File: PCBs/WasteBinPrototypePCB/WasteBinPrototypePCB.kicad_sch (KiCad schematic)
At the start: 31 parts, among them J1 Jack-DC 12V, J2 Conn_01x10_Male, J3 Conn_01x06_Male, J4 SM04B-SRSS-TB(LF)(SN), Q1 MMBT3904, Q2 IRL540NSTRLPBF, U1 PC817, U2 TLV1117-50, U3 ESP32-C3-DEVKITC-02, U4 A1301EUA-T

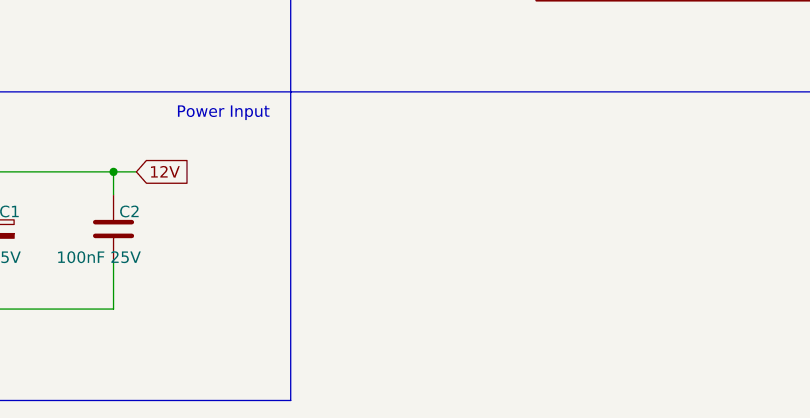
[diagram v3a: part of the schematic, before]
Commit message: created pcb board outline, layed out components and starting retouing wires.
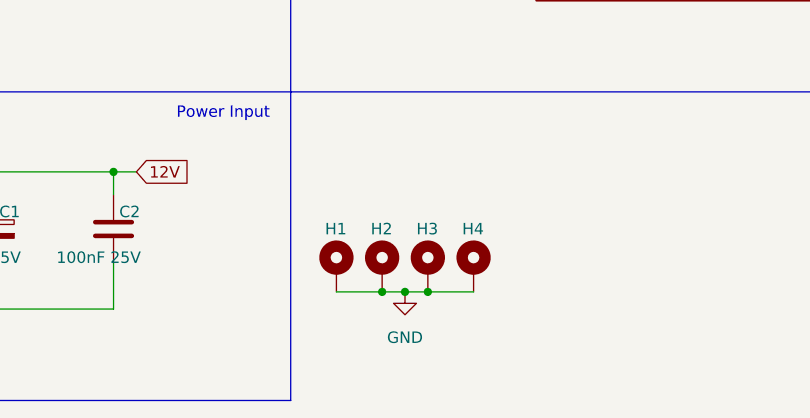
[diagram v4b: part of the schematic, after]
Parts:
- added H1, H2, H3, H4: MountingHole_Pad, MountingHole:MountingHole_3.2mm_M3, symbol Mechanical:MountingHole_Pad
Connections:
- net GND: now also H1.1, H2.1, H3.1, H4.1
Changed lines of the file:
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@@
     (comment 2 "Designed for Insyte Technology")
   )
+  (junction (at 114.3 118.11) (diameter 0) (color 0 0 0 0)
+  )
   (junction (at 52.07 120.015) (diameter 0) (color 0 0 0 0)
   )
@@
   (junction (at 165.1 83.185) (diameter 0) (color 0 0 0 0)
   )
+  (junction (at 111.76 118.11) (diameter 0) (color 0 0 0 0)
+  )
   (junction (at 66.04 120.015) (diameter 0) (color 0 0 0 0)
   )
@@
   (junction (at 81.915 74.295) (diameter 0) (color 0 0 0 0)
   )
+  (junction (at 109.22 118.11) (diameter 0) (color 0 0 0 0)
+  )
   (wire (pts (xy 53.975 43.815) (xy 55.88 43.815))
     (stroke (width 0) (type default) (color 0 0 0 0))
@@
     (stroke (width 0) (type default) (color 0 0 0 0))
   )
+  (wire (pts (xy 111.76 118.11) (xy 114.3 118.11))
+    (stroke (width 0) (type default) (color 0 0 0 0))
+  )
   (wire (pts (xy 38.1 120.015) (xy 38.1 109.855))
     (stroke (width 0) (type default) (color 0 0 0 0))
@@
     (stroke (width 0) (type default) (color 0 0 0 0))
   )
+  (wire (pts (xy 114.3 118.11) (xy 119.38 118.11))
+    (stroke (width 0) (type default) (color 0 0 0 0))
+  )
   (wire (pts (xy 79.375 104.775) (xy 81.915 104.775))
     (stroke (width 0) (type default) (color 0 0 0 0))
@@
     (stroke (width 0) (type default) (color 0 0 0 0))
   )
+  (wire (pts (xy 109.22 118.11) (xy 111.76 118.11))
+    (stroke (width 0) (type default) (color 0 0 0 0))
+  )
   (wire (pts (xy 67.31 16.51) (xy 67.31 20.955))
     (stroke (width 0) (type default) (color 0 0 0 0))
@@
   )
   (wire (pts (xy 32.385 33.655) (xy 45.085 33.655))
+    (stroke (width 0) (type default) (color 0 0 0 0))
+  )
+  (wire (pts (xy 104.14 118.11) (xy 109.22 118.11))
     (stroke (width 0) (type default) (color 0 0 0 0))
   )
@@
     (pin "2")
   )
+  (symbol (lib_id "power:GND") (at 111.76 118.11 0) (unit 1)
+    (in_bom yes) (on_board yes) (fields_autoplaced)
+    (property "Reference" "#PWR0101" (id 0) (at 111.76 124.46 0)
+      (effects (font (size 1.27 1.27)) hide)
+    )
+    (property "Value" "GND" (id 1) (at 111.76 123.19 0))
+    (property "Footprint" "" (id 2) (at 111.76 118.11 0)
+      (effects (font (size 1.27 1.27)) hide)
+    )
+    (property "Datasheet" "" (id 3) (at 111.76 118.11 0)
+      (effects (font (size 1.27 1.27)) hide)
+    )
+    (pin "1")
+  )
   (symbol (lib_id "Device:C") (at 133.35 27.94 180) (unit 1)
     (in_bom yes) (on_board yes)
@@
     (pin "S2")
   )
+  (symbol (lib_id "Mechanical:MountingHole_Pad") (at 114.3 115.57 0) (unit 1)
+    (in_bom yes) (on_board yes)
+    (property "Reference" "H3" (id 0) (at 113.03 111.125 0)
+      (effects (font (size 1.27 1.27)) (justify left))
+    )
+    (property "Value" "MountingHole_Pad" (id 1) (at 117.475 115.5699 0)
+      (effects (font (size 1.27 1.27)) (justify left) hide)
+    )
+    (property "Footprint" "MountingHole:MountingHole_3.2mm_M3" (id 2) (at 114.3 115.57 0)
+      (effects (font (size 1.27 1.27)) hide)
+    )
+    (property "Datasheet" "~" (id 3) (at 114.3 115.57 0)
+      (effects (font (size 1.27 1.27)) hide)
+    )
+    (pin "1")
+  )
   (symbol (lib_name "DIODE-1N4148_1") (lib_id "SparkFun-DiscreteSemi:DIODE-1N4148") (at 23.495 25.4 90) (unit 1)
     (in_bom yes) (on_board yes)
@@
     (pin "A")
     (pin "K")
+  )
+  (symbol (lib_id "Mechanical:MountingHole_Pad") (at 119.38 115.57 0) (unit 1)
+    (in_bom yes) (on_board yes)
+    (property "Reference" "H4" (id 0) (at 118.11 111.125 0)
+      (effects (font (size 1.27 1.27)) (justify left))
+    )
+    (property "Value" "MountingHole_Pad" (id 1) (at 122.555 115.5699 0)
+      (effects (font (size 1.27 1.27)) (justify left) hide)
+    )
+    (property "Footprint" "MountingHole:MountingHole_3.2mm_M3" (id 2) (at 119.38 115.57 0)
+      (effects (font (size 1.27 1.27)) hide)
+    )
+    (property "Datasheet" "~" (id 3) (at 119.38 115.57 0)
+      (effects (font (size 1.27 1.27)) hide)
+    )
+    (pin "1")
+  )
+  (symbol (lib_id "Mechanical:MountingHole_Pad") (at 104.14 115.57 0) (unit 1)
+    (in_bom yes) (on_board yes)
+    (property "Reference" "H1" (id 0) (at 102.87 111.125 0)
+      (effects (font (size 1.27 1.27)) (justify left))
+    )
+    (property "Value" "MountingHole_Pad" (id 1) (at 107.315 115.5699 0)
+      (effects (font (size 1.27 1.27)) (justify left) hide)
+    )
+    (property "Footprint" "MountingHole:MountingHole_3.2mm_M3" (id 2) (at 104.14 115.57 0)
+      (effects (font (size 1.27 1.27)) hide)
+    )
+    (property "Datasheet" "~" (id 3) (at 104.14 115.57 0)
+      (effects (font (size 1.27 1.27)) hide)
+    )
+    (pin "1")
   )
   (symbol (lib_id "Connector:Conn_01x10_Male") (at 146.05 26.67 0) (unit 1)
@@
     (pin "2")
     (pin "3")
+  )
+  (symbol (lib_id "Mechanical:MountingHole_Pad") (at 109.22 115.57 0) (unit 1)
+    (in_bom yes) (on_board yes)
+    (property "Reference" "H2" (id 0) (at 107.95 111.125 0)
+      (effects (font (size 1.27 1.27)) (justify left))
+    )
+    (property "Value" "MountingHole_Pad" (id 1) (at 112.395 115.5699 0)
+      (effects (font (size 1.27 1.27)) (justify left) hide)
+    )
+    (property "Footprint" "MountingHole:MountingHole_3.2mm_M3" (id 2) (at 109.22 115.57 0)
+      (effects (font (size 1.27 1.27)) hide)
+    )
+    (property "Datasheet" "~" (id 3) (at 109.22 115.57 0)
+      (effects (font (size 1.27 1.27)) hide)
+    )
+    (pin "1")
   )
   (symbol (lib_id "SamacSys_Parts:ESD7351HT1G") (at 202.565 29.21 270) (unit 1)
@@
       (reference "#PWR012") (unit 1) (value "GND") (footprint "")
     )
+    (path "/223b6225-b433-49b0-8472-9a3dc8eaebc0"
+      (reference "#PWR0101") (unit 1) (value "GND") (footprint "")
+    )
     (path "/eaf99cde-864a-43b8-ae61-a851944226d1"
       (reference "C1") (unit 1) (value "680uF 25V") (footprint "Capacitor_SMD:CP_Elec_8x10")
@@
       (reference "F1") (unit 1) (value "7A") (footprint "Fuse:Fuse_2010_5025Metric_Pad1.52x2.65mm_HandSolder")
     )
+    (path "/a7e74b27-99d4-4851-b597-0cf6c1a45cf9"
+      (reference "H1") (unit 1) (value "MountingHole_Pad") (footprint "MountingHole:MountingHole_3.2mm_M3")
+    )
+    (path "/dbb2dcaf-494a-45f4-838a-5f62baed2fcc"
+      (reference "H2") (unit 1) (value "MountingHole_Pad") (footprint "MountingHole:MountingHole_3.2mm_M3")
+    )
+    (path "/4fd399a7-d7fd-42c7-95c2-080617db2272"
+      (reference "H3") (unit 1) (value "MountingHole_Pad") (footprint "MountingHole:MountingHole_3.2mm_M3")
+    )
+    (path "/a14b9400-d662-495c-9a20-54cecbeb2b96"
+      (reference "H4") (unit 1) (value "MountingHole_Pad") (footprint "MountingHole:MountingHole_3.2mm_M3")
+    )
     (path "/c46440ce-3f40-47ae-a5ee-add879bfd473"

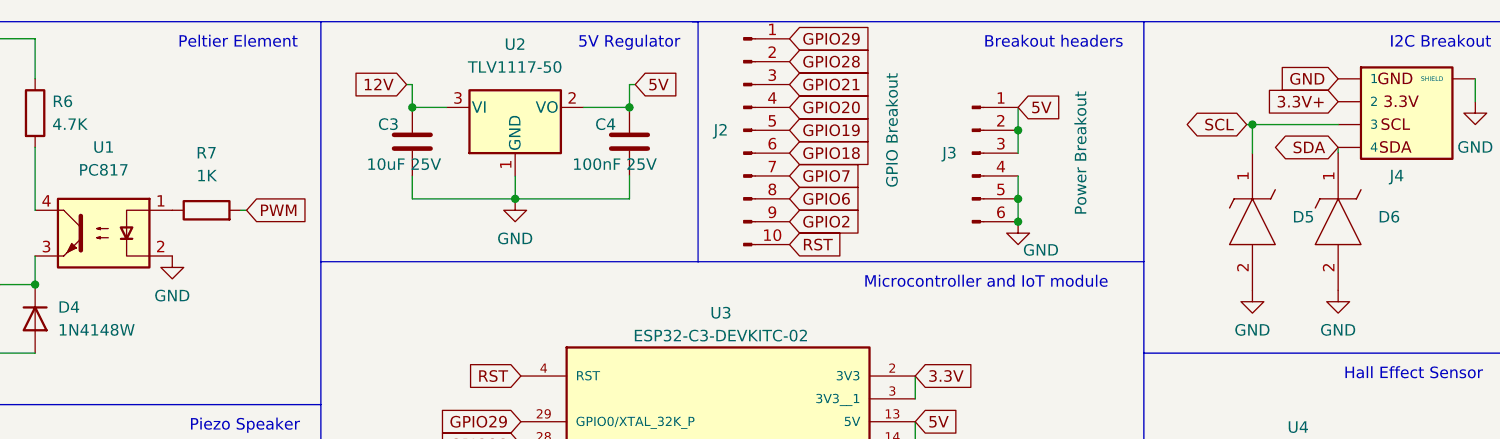
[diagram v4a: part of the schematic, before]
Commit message: finished wiring and added silkscreen.
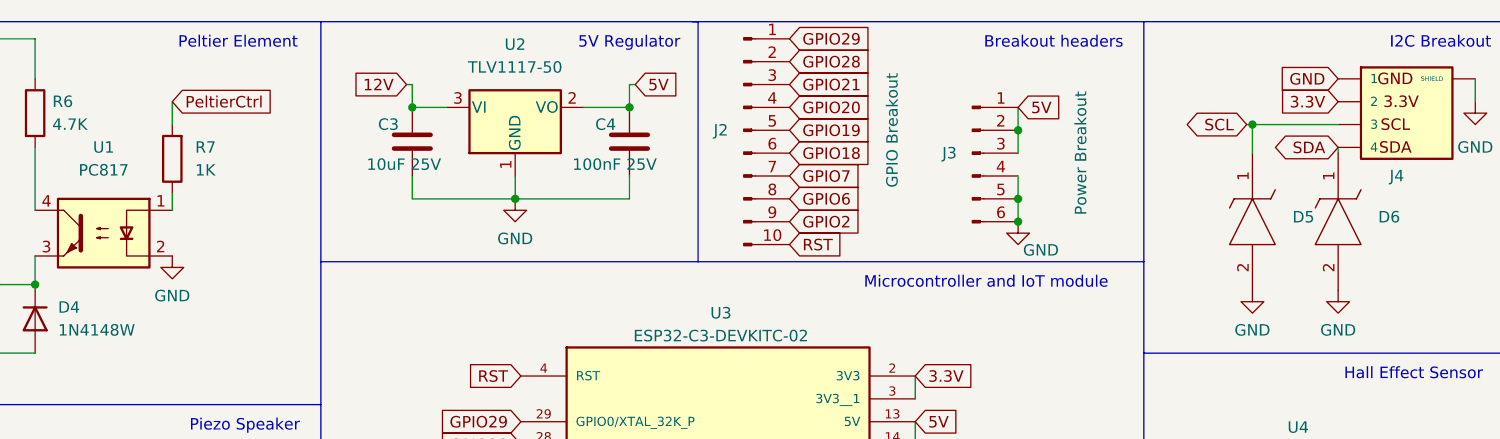
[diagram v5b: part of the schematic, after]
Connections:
- net 3.3V+ is gone; now on net 3.3V: J4.2
- net PWM is gone; now on net PeltierCtrl: R7.2
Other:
- moved on the sheet: R7
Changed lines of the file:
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@@
+    (stroke (width 0) (type default) (color 0 0 0 0))
+  )
+  (wire (pts (xy 82.55 33.655) (xy 82.55 35.56))
     (stroke (width 0) (type default) (color 0 0 0 0))
   )
@@
     (stroke (width 0) (type default) (color 0 0 0 0))
   )
+  (wire (pts (xy 82.55 23.495) (xy 82.55 26.035))
+    (stroke (width 0) (type default) (color 0 0 0 0))
+  )
   (wire (pts (xy 79.375 104.775) (xy 81.915 104.775))
     (stroke (width 0) (type default) (color 0 0 0 0))
@@
   )
   (wire (pts (xy 32.385 16.51) (xy 23.495 16.51))
-    (stroke (width 0) (type default) (color 0 0 0 0))
-  )
-  (wire (pts (xy 90.805 35.56) (xy 90.17 35.56))
     (stroke (width 0) (type default) (color 0 0 0 0))
   )
@@
     (effects (font (size 1.27 1.27)) (justify left bottom))
   )
-  (global_label "3.3V+" (shape input) (at 212.09 23.495 180) (fields_autoplaced)
-    (effects (font (size 1.27 1.27)) (justify right))
-    (property "Intersheet References" "${INTERSHEET_REFS}" (id 0) (at 203.9921 23.5744 0)
+  (global_label "3.3V" (shape input) (at 212.09 23.495 180) (fields_autoplaced)
+    (effects (font (size 1.27 1.27)) (justify right))
+    (property "Intersheet References" "${INTERSHEET_REFS}" (id 0) (at 205.5645 23.4156 0)
       (effects (font (size 1.27 1.27)) (justify right) hide)
     )
@@
     )
   )
+  (global_label "PeltierCtrl" (shape input) (at 82.55 23.495 0) (fields_autoplaced)
+    (effects (font (size 1.27 1.27)) (justify left))
+    (property "Intersheet References" "${INTERSHEET_REFS}" (id 0) (at 94.6393 23.5744 0)
+      (effects (font (size 1.27 1.27)) (justify left) hide)
+    )
+  )
   (global_label "SCL" (shape bidirectional) (at 121.285 81.915 180) (fields_autoplaced)
     (effects (font (size 1.27 1.27)) (justify right))
@@
     (effects (font (size 1.27 1.27)) (justify left))
     (property "Intersheet References" "${INTERSHEET_REFS}" (id 0) (at 159.2279 34.3694 0)
-      (effects (font (size 1.27 1.27)) (justify left) hide)
-    )
-  )
-  (global_label "PWM" (shape input) (at 90.805 35.56 0) (fields_autoplaced)
-    (effects (font (size 1.27 1.27)) (justify left))
-    (property "Intersheet References" "${INTERSHEET_REFS}" (id 0) (at 97.391 35.4806 0)
       (effects (font (size 1.27 1.27)) (justify left) hide)
     )
@@
     (pin "9")
   )
-  (symbol (lib_id "Device:R") (at 86.36 35.56 90) (unit 1)
-    (in_bom yes) (on_board yes) (fields_autoplaced)
-    (property "Reference" "R7" (id 0) (at 86.36 29.21 90))
-    (property "Value" "1K" (id 1) (at 86.36 31.75 90))
-    (property "Footprint" "Resistor_SMD:R_0805_2012Metric_Pad1.20x1.40mm_HandSolder" (id 2) (at 86.36 37.338 90)
-      (effects (font (size 1.27 1.27)) hide)
-    )
-    (property "Datasheet" "~" (id 3) (at 86.36 35.56 0)
-      (effects (font (size 1.27 1.27)) hide)
-    )
+  (symbol (lib_id "Device:R") (at 82.55 29.845 180) (unit 1)
+    (in_bom yes) (on_board yes) (fields_autoplaced)
+    (property "Reference" "R7" (id 0) (at 85.09 28.5749 0)
+      (effects (font (size 1.27 1.27)) (justify right))
+    )
+    (property "Value" "1K" (id 1) (at 85.09 31.1149 0)
+      (effects (font (size 1.27 1.27)) (justify right))
+    )
+    (property "Footprint" "Resistor_SMD:R_0805_2012Metric_Pad1.20x1.40mm_HandSolder" (id 2) (at 84.328 29.845 90)
+      (effects (font (size 1.27 1.27)) hide)
+    )
+    (property "Datasheet" "~" (id 3) (at 82.55 29.845 0)
+      (effects (font (size 1.27 1.27)) hide)
+    )
